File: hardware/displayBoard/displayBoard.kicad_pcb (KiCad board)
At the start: 2 copper layers, 55 x 55 mm, 33 parts, among them J1 Conn_01x10_Pin, Q1 MMBTA42, Q10 MMBTA42, Q11 BSS123, Q2 MMBTA42, Q3 MMBTA42, Q4 MMBTA42, Q5 MMBTA42, Q6 MMBTA42, Q7 MMBTA42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

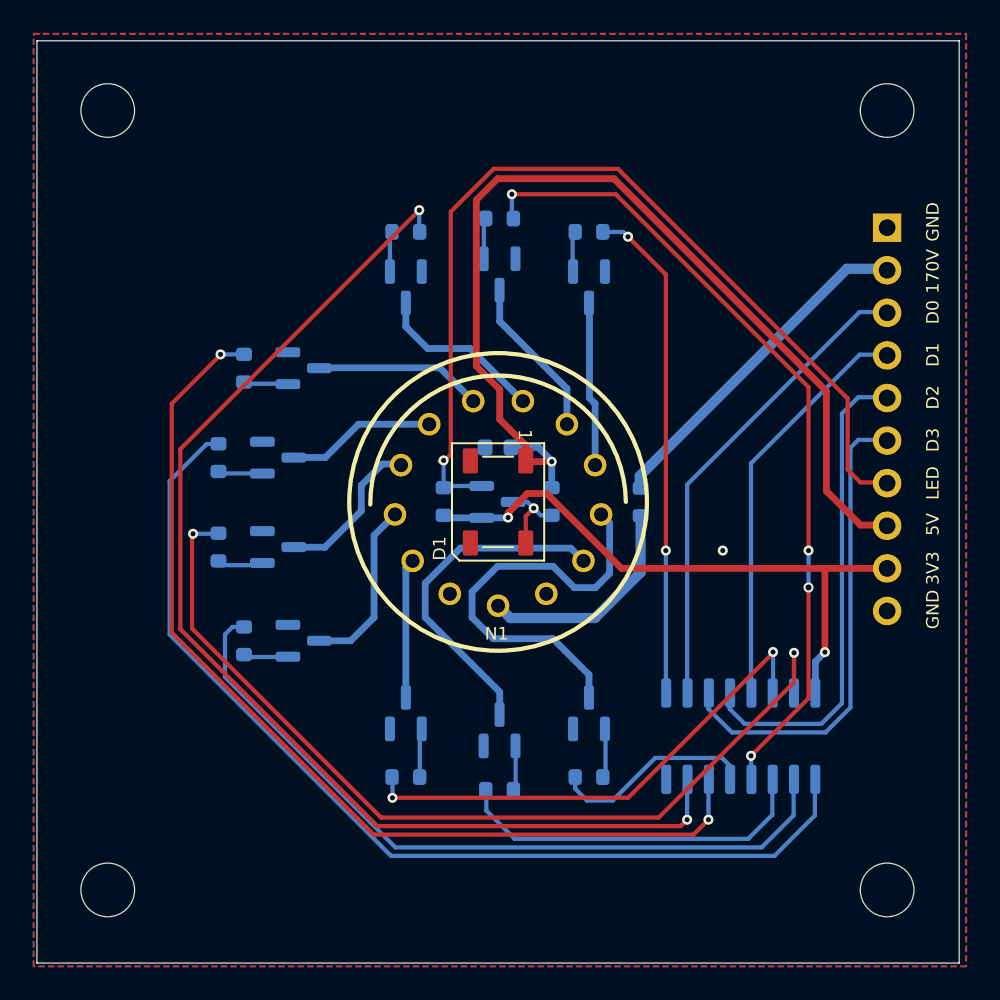
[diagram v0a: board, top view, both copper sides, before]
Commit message: Add pull-ups to BCD decoder inputs
- Add pull-up resistors to BCD decoder to prevent turning on the nixie tube during boot
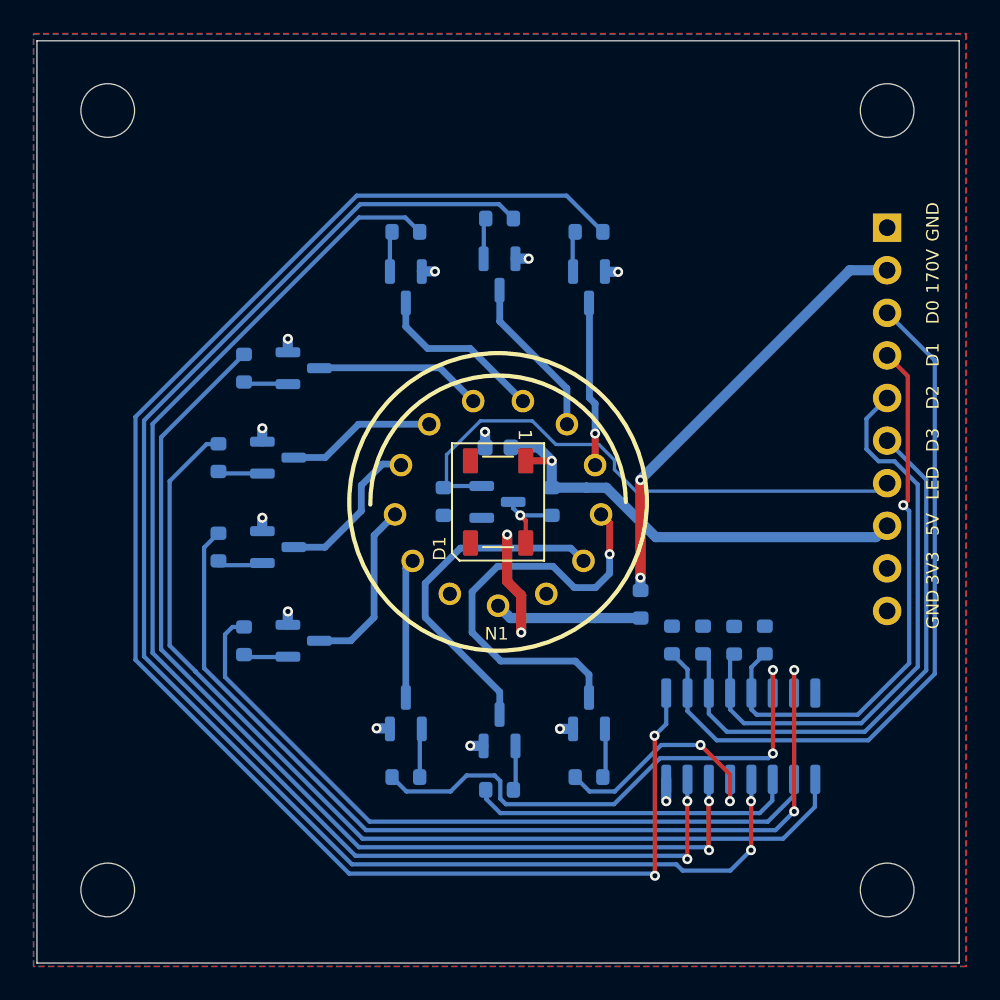
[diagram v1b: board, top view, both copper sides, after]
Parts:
- added R14: 18k, Resistor_SMD:R_0603_1608Metric, B.Cu at (158.9, 113.2)
- added R15: 18k, Resistor_SMD:R_0603_1608Metric, B.Cu at (164.4, 113.2)
- added R16: 18k, Resistor_SMD:R_0603_1608Metric, B.Cu at (162.6, 113.3)
- added R17: 18k, Resistor_SMD:R_0603_1608Metric, B.Cu at (160.7, 113.2)
- moved R12 6.10 mm to (157.0, 111.1)
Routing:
- net /DIG8: track 29.2 -> 96.3 mm
- net /DIG7: track 49.2 -> 88.1 mm, vias 4 -> 2
- net +5V: track 59.6 -> 27.4 mm
- net +3V3: track 36.2 -> 6.18 mm
- net /LED: track 56.5 -> 34.2 mm, vias 1 -> 0
- net /D0: track 28.3 -> 43.6 mm
- net GND: track 0.00 -> 9.98 mm, vias 1 -> 12
- net /D1: track 24.2 -> 33.6 mm, vias 0 -> 1
- net /DIG6: track 69.5 -> 76.8 mm
- net VCC: track 20.8 -> 26.5 mm, vias 0 -> 2
- net /D2: track 29.5 -> 34.7 mm
- net /D3: track 29.1 -> 33.3 mm
- net Net-(N1-PadA): track 12.8 -> 8.81 mm
- net /DIG3: track 54.7 -> 57.8 mm
- net /DIG5: track 58.4 -> 61.5 mm
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- added copper zone on B.Cu, net +3V3
- removed copper zone on B.Cu, net GND
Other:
- board text added: "Single digit nixie clock - Display board Daniel Knežević 2025"
- board text removed: "Single digit nixie clock - Display board Daniel Knežević 2024"

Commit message: Add a decoupling cap to CD4028
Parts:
- added C2: 100n, Capacitor_SMD:C_0603_1608Metric, B.Cu at (167.4, 113.2)
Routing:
- net GND: track 9.98 -> 10.9 mm, vias 12 -> 13
- net /NIXIE3: track 8.94 -> 8.05 mm
- net /NIXIE9: track 25.1 -> 24.4 mm
- net /NIXIE0: track 20.1 -> 19.5 mm
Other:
- board text added: "Single digit nixie clock - Display board v2 Daniel Knežević 2025"
- board text removed: "Single digit nixie clock - Display board Daniel Knežević 2025"

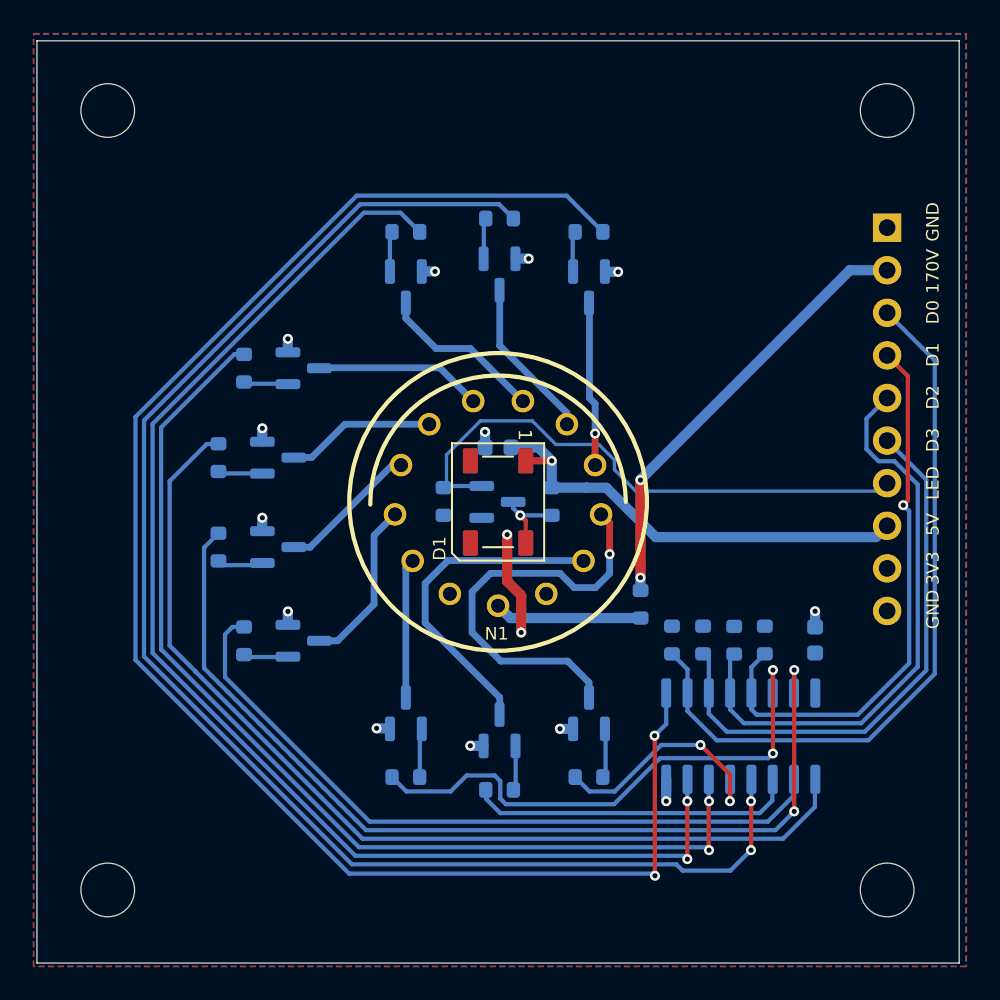
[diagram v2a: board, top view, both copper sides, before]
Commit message: Add copper thief to the bottom layer of display board
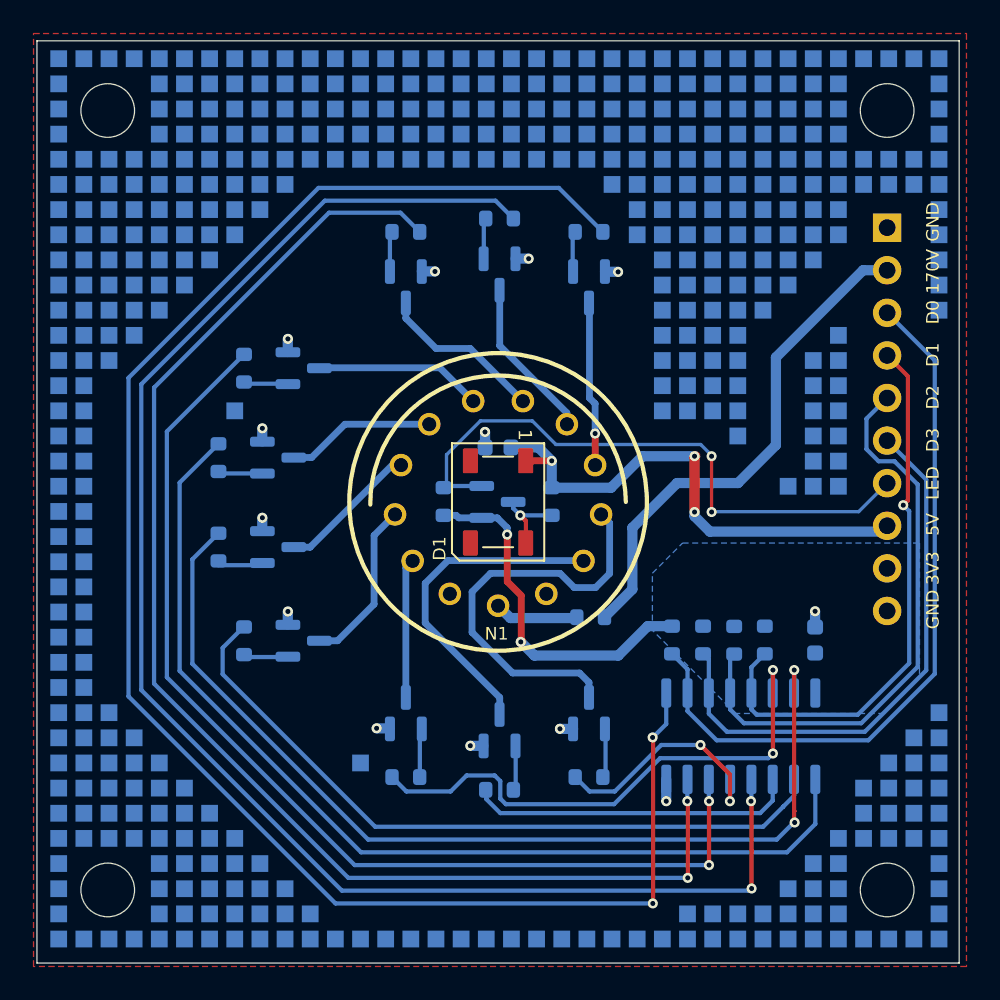
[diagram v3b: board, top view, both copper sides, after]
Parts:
- moved R12 3.08 mm to (154.0, 111.9), turned to 0 degrees
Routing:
- net +3V3: track 6.18 -> 21.3 mm
- net /DIG8: track 96.3 -> 102.8 mm
- net /DIG7: track 88.1 -> 93.2 mm
- net VCC: track 26.5 -> 30.6 mm, vias 2 -> 0
- net Net-(N1-PadA): track 8.81 -> 5.02 mm
- net /DIG6: track 77.0 -> 80.8 mm
- net /LED: track 34.2 -> 37.8 mm, vias 0 -> 2
- net +5V: track 27.4 -> 30.8 mm, vias 1 -> 3
- net /DIG3: track 57.8 -> 59.6 mm
- net /DIG5: track 61.8 -> 63.3 mm
- net /DIG4: track 58.7 -> 59.9 mm
- net /DIG2: track 42.4 -> 43.1 mm
- net /DIG0: track 18.7 -> 19.2 mm
- net /NIXIE9: vias 1 -> 0
